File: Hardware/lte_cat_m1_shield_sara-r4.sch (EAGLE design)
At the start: 77 parts, among them J8 NANO_SIM, J9 U.FL, Q1 2.5A/30V/105mΩ, Q2 600mA/40V, U1 TXB0104, U2 3.3V, U3 MCP73831, U4 AP7361C-33FGE, U5 SARA-R4

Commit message: Minor revisions post-review
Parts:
- JP2: device SparkFun-Jumpers:JUMPER-SMT_3_NO_NO-SILK -> SparkFun-Jumpers:JUMPER-SMT_3_NO_SILK
- JP3, JP4, JP5, JP6: value JUMPER-SMT_2_NC_TRACE_NO-SILK -> JUMPER-SMT_2_NC_TRACE_SILK; device SparkFun-Jumpers:JUMPER-SMT_2_NC_TRACE_NO-SILK -> SparkFun-Jumpers:JUMPER-SMT_2_NC_TRACE_SILK
- JP7: device SparkFun-Jumpers:JUMPER-SMT_2_NO_NO-SILK -> SparkFun-Jumpers:JUMPER-SMT_2_NO_SILK
- U5: value SARA-R4 -> SARA-R410M-2B
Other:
- note added: "Hardware Serial Port (D0 = RX, D1 = TX)"
- note added: "If the Arduino does not supply IOREF, Use JP2 to set it to either 5V or 3.3V."
- note added: "Software serial port (D8 = RX, D9 = TX)"
- note removed: "If the Arduino does not supply IOREF, Use JP??? to set it to either 5V or 3.3V."
- moved on the sheet: C7, D3, R6, S1

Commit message: hardware revisions post u-blox review - x02 production hardware
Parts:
- R1: value 10k -> 47k; device SparkFun-Resistors:10KOHM-0603-1/10W-1% -> SparkFun-Resistors:47KOHM-0603-1/10W-1%
- U2: value 3.3V -> AP2112K-3.3
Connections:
- net D_N renamed D+
- net D_P renamed D-
- net GND: now also U5.RSVD@33
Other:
- note added: "Molex 146208 chip antenna peak gain: 698~960MHz: 0.2 dBi 1.7~2.7GHz: 3.8 dBi"
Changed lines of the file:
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@@
 <part name="GND41" library="SparkFun-PowerSymbols" deviceset="GND" device=""/>
 <part name="B1" library="SparkFun-Boards" deviceset="ARDUINO_UNO_R3_SHIELD" device="NOLABELS"/>
-<part name="U2" library="SparkFun-IC-Power" deviceset="V_REG_AP2112" device="K-3.3V" value="3.3V"/>
+<part name="U2" library="SparkFun-IC-Power" deviceset="V_REG_AP2112" device="K-3.3V" value="AP2112K-3.3"/>
 <part name="C2" library="SparkFun-Capacitors" deviceset="1.0UF" device="-0603-16V-10%" value="1.0uF"/>
 <part name="C4" library="SparkFun-Capacitors" deviceset="1.0UF" device="-0603-16V-10%" value="1.0uF"/>
 <part name="GND2" library="SparkFun-PowerSymbols" deviceset="GND" device=""/>
 <part name="GND9" library="SparkFun-PowerSymbols" deviceset="GND" device=""/>
-<part name="R1" library="SparkFun-Resistors" deviceset="10KOHM" device="-0603-1/10W-1%" value="10k"/>
+<part name="R1" library="SparkFun-Resistors" deviceset="47KOHM" device="-0603-1/10W-1%" value="47k"/>
 <part name="GND5" library="SparkFun-PowerSymbols" deviceset="GND" device=""/>
 <part name="GND6" library="SparkFun-PowerSymbols" deviceset="GND" device=""/>
@@
 </segment>
 </net>
-<net name="D_N" class="1">
+<net name="D+" class="1">
 <segment>
 <pinref part="D5" gate="G$1" pin="6"/>
@@
 </segment>
 </net>
-<net name="D_P" class="1">
+<net name="D-" class="1">
 <segment>
 <pinref part="D5" gate="G$1" pin="4"/>
@@
 SARA module are w/ respect
 to DTE (Arduino).</text>
+<text x="149.86" y="167.64" size="1.778" layer="97">Molex 146208 chip antenna peak gain:
+698~960MHz: 0.2 dBi
+1.7~2.7GHz: 3.8 dBi</text>
 </plain>
 <instances>
@@
 <instance part="S4" gate="G$1" x="33.02" y="121.92" rot="R90"/>
 <instance part="SUPPLY15" gate="G$1" x="63.5" y="22.86"/>
-<instance part="GND27" gate="1" x="63.5" y="68.58"/>
+<instance part="GND27" gate="1" x="63.5" y="58.42"/>
 <instance part="SUPPLY14" gate="G$1" x="60.96" y="142.24"/>
 <instance part="J8" gate="G$1" x="241.3" y="81.28"/>
@@
 <pinref part="U5" gate="G$1" pin="GND"/>
 <pinref part="GND27" gate="1" pin="GND"/>
-<wire x1="66.04" y1="73.66" x2="63.5" y2="73.66" width="0.1524" layer="91"/>
-<wire x1="63.5" y1="73.66" x2="63.5" y2="71.12" width="0.1524" layer="91"/>
+<wire x1="66.04" y1="63.5" x2="63.5" y2="63.5" width="0.1524" layer="91"/>
+<wire x1="63.5" y1="63.5" x2="63.5" y2="60.96" width="0.1524" layer="91"/>
+<pinref part="U5" gate="G$1" pin="RSVD@33"/>
+<wire x1="66.04" y1="68.58" x2="63.5" y2="68.58" width="0.1524" layer="91"/>
+<wire x1="63.5" y1="68.58" x2="63.5" y2="63.5" width="0.1524" layer="91"/>
+<junction x="63.5" y="63.5"/>
 </segment>
 <segment>
@@
 </segment>
 </net>
-<net name="D_N" class="1">
+<net name="D+" class="1">
 <segment>
 <pinref part="U5" gate="G$1" pin="USB_D-"/>
@@
 </segment>
 </net>
-<net name="D_P" class="1">
+<net name="D-" class="1">
 <segment>
 <pinref part="U5" gate="G$1" pin="USB_D+"/>

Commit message: v10 of the LTE Shield hardware.
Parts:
- removed U1: TXB0104, SparkFun-IC-Comms:TXB0104PWRSOIC14
- added U6: TCA9406DCU, ublox:TCA9406DCU
- added U8: TXB0104, SparkFun-IC-Comms:TXB0104PWR
- LOGO1: value SPARKX-LOGO4 -> SFE_LOGO_NAME.2_INCH; device SparkX:SPARKX-LOGO4 -> SparkFun-Aesthetics:SFE_LOGO_NAME.2_INCH
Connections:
- removed net GPIO3: J4.1, U5.GPIO3
- new net GPIO3-CELL: U5.GPIO3, U8.A1
- new net GPIO3-QWIIC: J4.1, U8.B1
- net 1.8V: now also U6.OE, U6.VCCA, U8.OE, U8.VCCA; no longer U1.OE, U1.VCCA
- net D+: now also D5.4, U5.USB_D+; no longer D5.6, U5.USB_D-
- net D-: now also D5.6, U5.USB_D-; no longer D5.4, U5.USB_D+
- net GND: now also U6.GND, U8.GND; no longer U1.GND
- net IOREF: now also U6.VCCB, U8.VCCB; no longer U1.VCCB
- net RX-ARDUINO: now also U8.B2; no longer U1.B3
- net RX-CELL: now also U8.A3; no longer U1.A4
- net SCL-CELL: now also U6.SCL_A; no longer U1.A1
- net SCL-QWIIC: now also U6.SCL_B; no longer U1.B1
- net SDA-CELL: now also U6.SDA_A; no longer U1.A2
- net SDA-QWIIC: now also U6.SDA_B; no longer U1.B2
- net TX-ARDUINO: now also U8.B3; no longer U1.B4
- net TX-CELL: now also U8.A2; no longer U1.A3
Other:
- note added: "GPIO3 is an optional interrupt output from the GPS module to the SARA module."
- note added: "v10"
- note removed: "GPIO3 is an (optional?) interrupt output from the GPS module to the SARA module."
- note removed: "x01"
- moved on the sheet: B1, C1, C3, J5, JP2, JP3, JP4, S1

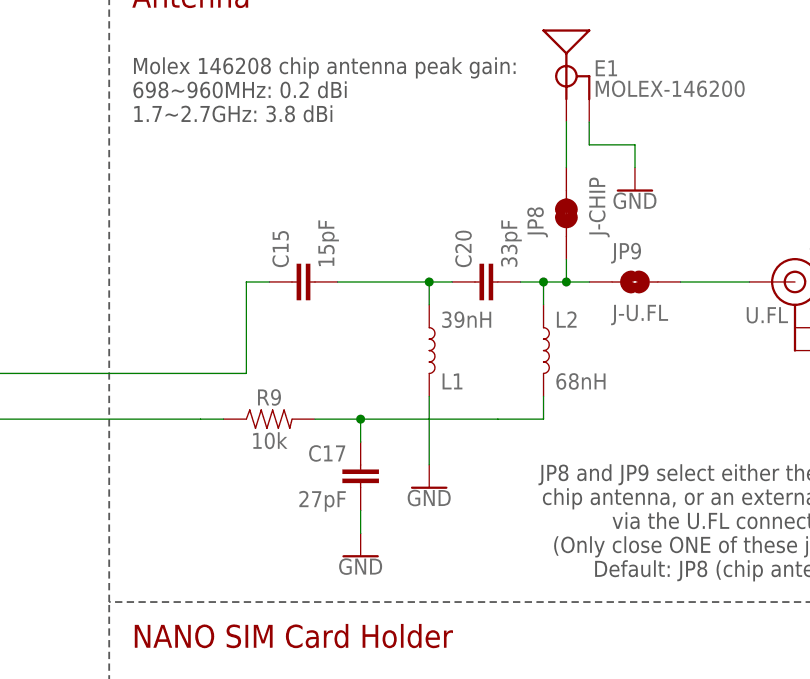
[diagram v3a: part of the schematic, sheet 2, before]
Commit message: DNP'ing the antenna-detect circuit.
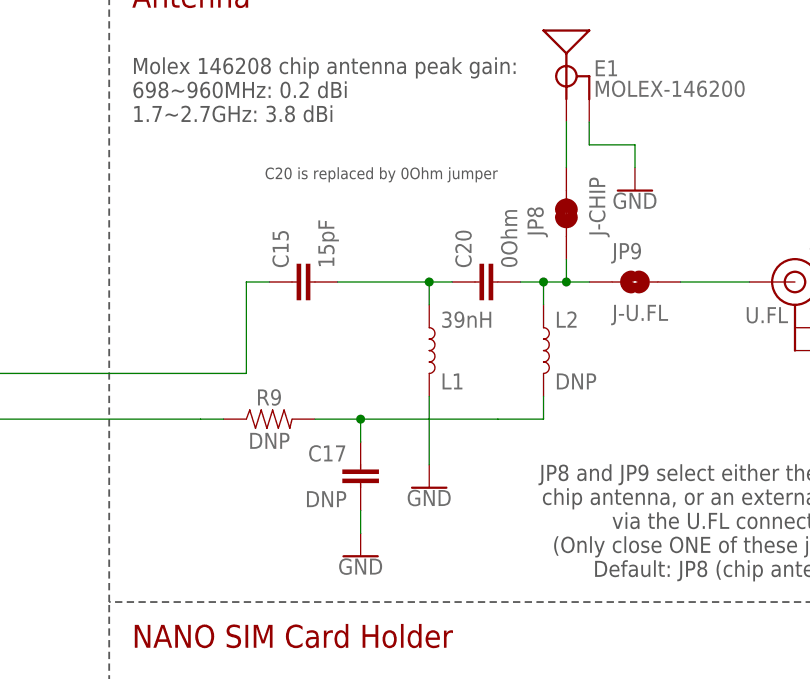
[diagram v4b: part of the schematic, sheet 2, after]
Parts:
- C17: value 27pF -> DNP
- C20: value 33pF -> 0Ohm
- L2: value 68nH -> DNP
- R9: value 10k -> DNP
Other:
- note added: "C20 is replaced by 0Ohm jumper"
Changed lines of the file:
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@@
 <grid distance="0.1" unitdist="inch" unit="inch" style="lines" multiple="1" display="no" altdistance="0.01" altunitdist="inch" altunit="inch"/>
 <layers>
-<layer number="1" name="Top" color="4" fill="1" visible="yes" active="no"/>
-<layer number="2" name="Route2" color="1" fill="3" visible="yes" active="no"/>
-<layer number="15" name="Route15" color="4" fill="6" visible="yes" active="no"/>
-<layer number="16" name="Bottom" color="1" fill="1" visible="yes" active="no"/>
-<layer number="17" name="Pads" color="2" fill="1" visible="yes" active="no"/>
-<layer number="18" name="Vias" color="2" fill="1" visible="yes" active="no"/>
-<layer number="19" name="Unrouted" color="6" fill="1" visible="yes" active="no"/>
-<layer number="20" name="Dimension" color="15" fill="1" visible="yes" active="no"/>
-<layer number="21" name="tPlace" color="16" fill="1" visible="yes" active="no"/>
-<layer number="22" name="bPlace" color="14" fill="1" visible="yes" active="no"/>
-<layer number="23" name="tOrigins" color="15" fill="1" visible="yes" active="no"/>
-<layer number="24" name="bOrigins" color="15" fill="1" visible="yes" active="no"/>
-<layer number="25" name="tNames" color="7" fill="1" visible="yes" active="no"/>
-<layer number="26" name="bNames" color="7" fill="1" visible="yes" active="no"/>
-<layer number="27" name="tValues" color="7" fill="1" visible="yes" active="no"/>
-<layer number="28" name="bValues" color="7" fill="1" visible="yes" active="no"/>
+<layer number="1" name="Top" color="4" fill="1" visible="no" active="no"/>
+<layer number="2" name="Route2" color="1" fill="3" visible="no" active="no"/>
+<layer number="15" name="Route15" color="4" fill="6" visible="no" active="no"/>
+<layer number="16" name="Bottom" color="1" fill="1" visible="no" active="no"/>
+<layer number="17" name="Pads" color="2" fill="1" visible="no" active="no"/>
+<layer number="18" name="Vias" color="2" fill="1" visible="no" active="no"/>
+<layer number="19" name="Unrouted" color="6" fill="1" visible="no" active="no"/>
+<layer number="20" name="Dimension" color="15" fill="1" visible="no" active="no"/>
+<layer number="21" name="tPlace" color="16" fill="1" visible="no" active="no"/>
+<layer number="22" name="bPlace" color="14" fill="1" visible="no" active="no"/>
+<layer number="23" name="tOrigins" color="15" fill="1" visible="no" active="no"/>
+<layer number="24" name="bOrigins" color="15" fill="1" visible="no" active="no"/>
+<layer number="25" name="tNames" color="7" fill="1" visible="no" active="no"/>
+<layer number="26" name="bNames" color="7" fill="1" visible="no" active="no"/>
+<layer number="27" name="tValues" color="7" fill="1" visible="no" active="no"/>
+<layer number="28" name="bValues" color="7" fill="1" visible="no" active="no"/>
 <layer number="29" name="tStop" color="7" fill="3" visible="no" active="no"/>
 <layer number="30" name="bStop" color="7" fill="6" visible="no" active="no"/>
@@
 <layer number="35" name="tGlue" color="7" fill="4" visible="no" active="no"/>
 <layer number="36" name="bGlue" color="7" fill="5" visible="no" active="no"/>
-<layer number="37" name="tTest" color="7" fill="1" visible="yes" active="no"/>
-<layer number="38" name="bTest" color="7" fill="1" visible="yes" active="no"/>
+<layer number="37" name="tTest" color="7" fill="1" visible="no" active="no"/>
+<layer number="38" name="bTest" color="7" fill="1" visible="no" active="no"/>
 <layer number="39" name="tKeepout" color="4" fill="11" visible="no" active="no"/>
 <layer number="40" name="bKeepout" color="1" fill="11" visible="no" active="no"/>
@@
 <layer number="44" name="Drills" color="7" fill="1" visible="no" active="no"/>
 <layer number="45" name="Holes" color="7" fill="1" visible="no" active="no"/>
-<layer number="46" name="Milling" color="3" fill="1" visible="yes" active="no"/>
-<layer number="47" name="Measures" color="7" fill="1" visible="yes" active="no"/>
-<layer number="48" name="Document" color="7" fill="1" visible="yes" active="no"/>
-<layer number="49" name="Reference" color="7" fill="1" visible="yes" active="no"/>
-<layer number="50" name="dxf" color="7" fill="1" visible="yes" active="no"/>
-<layer number="51" name="tDocu" color="6" fill="1" visible="yes" active="no"/>
-<layer number="52" name="bDocu" color="7" fill="1" visible="yes" active="no"/>
-<layer number="53" name="tGND_GNDA" color="7" fill="9" visible="yes" active="no"/>
-<layer number="54" name="bGND_GNDA" color="1" fill="9" visible="yes" active="no"/>
-<layer number="56" name="wert" color="7" fill="1" visible="yes" active="no"/>
-<layer number="57" name="tCAD" color="7" fill="1" visible="yes" active="no"/>
-<layer number="59" name="tCarbon" color="7" fill="1" visible="yes" active="no"/>
-<layer number="60" name="bCarbon" color="7" fill="1" visible="yes" active="no"/>
+<layer number="46" name="Milling" color="3" fill="1" visible="no" active="no"/>
+<layer number="47" name="Measures" color="7" fill="1" visible="no" active="no"/>
+<layer number="48" name="Document" color="7" fill="1" visible="no" active="no"/>
+<layer number="49" name="Reference" color="7" fill="1" visible="no" active="no"/>
+<layer number="50" name="dxf" color="7" fill="1" visible="no" active="no"/>
+<layer number="51" name="tDocu" color="6" fill="1" visible="no" active="no"/>
+<layer number="52" name="bDocu" color="7" fill="1" visible="no" active="no"/>
+<layer number="53" name="tGND_GNDA" color="7" fill="9" visible="no" active="no"/>
+<layer number="54" name="bGND_GNDA" color="1" fill="9" visible="no" active="no"/>
+<layer number="56" name="wert" color="7" fill="1" visible="no" active="no"/>
+<layer number="57" name="tCAD" color="7" fill="1" visible="no" active="no"/>
+<layer number="59" name="tCarbon" color="7" fill="1" visible="no" active="no"/>
+<layer number="60" name="bCarbon" color="7" fill="1" visible="no" active="no"/>
 <layer number="88" name="SimResults" color="9" fill="1" visible="yes" active="yes"/>
 <layer number="89" name="SimProbes" color="9" fill="1" visible="yes" active="yes"/>
@@
 <part name="GND34" library="SparkFun-PowerSymbols" deviceset="GND" device=""/>
 <part name="GND33" library="SparkFun-PowerSymbols" deviceset="GND" device=""/>
-<part name="C17" library="SparkFun-Capacitors" deviceset="27PF" device="-0603-50V-5%" value="27pF"/>
-<part name="R9" library="SparkFun-Resistors" deviceset="10KOHM" device="-0603-1/10W-1%" value="10k"/>
+<part name="C17" library="SparkFun-Capacitors" deviceset="27PF" device="-0603-50V-5%" value="DNP"/>
+<part name="R9" library="SparkFun-Resistors" deviceset="10KOHM" device="-0603-1/10W-1%" value="DNP"/>
 <part name="GND36" library="SparkFun-PowerSymbols" deviceset="GND" device=""/>
 <part name="C15" library="SparkFun-Capacitors" deviceset="15PF" device="-0603-50V-5%" value="15pF"/>
-<part name="C20" library="SparkFun-Capacitors" deviceset="33PF" device="-0603-50V-5%" value="33pF"/>
+<part name="C20" library="SparkFun-Capacitors" deviceset="33PF" device="-0603-50V-5%" value="0Ohm"/>
 <part name="GND42" library="SparkFun-PowerSymbols" deviceset="GND" device=""/>
 <part name="L1" library="ublox" deviceset="INDUCTOR" device="-0603-39NH" value="39nH"/>
 <part name="GND38" library="SparkFun-PowerSymbols" deviceset="GND" device=""/>
-<part name="L2" library="ublox" deviceset="INDUCTOR" device="-0603-68NH" value="68nH"/>
+<part name="L2" library="ublox" deviceset="INDUCTOR" device="-0603-68NH" value="DNP"/>
 <part name="Q2" library="SparkFun-DiscreteSemi" deviceset="TRANS_NPN" device="-MMBT2222AL" value="600mA/40V"/>
 <part name="SUPPLY21" library="SparkFun-PowerSymbols" deviceset="3.3V" device=""/>
@@
 698~960MHz: 0.2 dBi
 1.7~2.7GHz: 3.8 dBi</text>
+<text x="190.5" y="162.56" size="1.27" layer="97" rot="R180">C20 is replaced by 0Ohm jumper</text>
 </plain>
 <instances>

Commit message: Revisions post-checklist.
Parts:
- removed JP9: J-U.FL, SparkFun-Jumpers:JUMPER-SMT_2_NO_NO-SILK
- removed R9: DNP, SparkFun-Resistors:10KOHM-0603-1/10W-1%
- added JP1: IOREF-SEL, SparkFun-Jumpers:JUMPER-SMT_3_NO_SILK
- added LOGO3: SFE_LOGO_NAME.2_INCH, SparkFun-Aesthetics:SFE_LOGO_NAME.2_INCH
- added R4: 10k, SparkFun-Resistors:10KOHM-0603-1/10W-1%
- C1, C3: value 0.1uF -> 1.0uF; device SparkFun-Capacitors:0.1UF-0603-25V-(+80/-20%) -> SparkFun-Capacitors:1.0UF-0603-16V-10%
- C16: value 47pF -> DNP; device SparkFun-Capacitors:47PF-0603-50V-5% -> SparkFun-Capacitors:27PF-0603-50V-5%
- C17: value DNP -> 47pF; device SparkFun-Capacitors:27PF-0603-50V-5% -> SparkFun-Capacitors:47PF-0603-50V-5%
- C19: value 47pF -> 0Ohm; device SparkFun-Capacitors:47PF-0603-50V-5% -> SparkFun-Capacitors:33PF-0603-50V-5%
- C2, C4: value 1.0uF -> 0.1uF; device SparkFun-Capacitors:1.0UF-0603-16V-10% -> SparkFun-Capacitors:0.1UF-0603-25V-(+80/-20%)
- C20: value 0Ohm -> 47pF; device SparkFun-Capacitors:33PF-0603-50V-5% -> SparkFun-Capacitors:47PF-0603-50V-5%
- D1: value Yellow -> PRTR5V0U2F; device SparkFun-LED:LED-YELLOW0603 -> ublox:PRTR5V0U2F
- D2: value 1A/23V/620mV -> Yellow; device SparkFun-DiscreteSemi:DIODE-SCHOTTKY-BAT20J -> SparkFun-LED:LED-YELLOW0603
- D3: value RED -> 1A/23V/620mV; device SparkFun-LED:LED-RED0603 -> SparkFun-DiscreteSemi:DIODE-SCHOTTKY-BAT20J
- D4: value BLUE -> RED; device SparkFun-LED:LED-BLUE0603 -> SparkFun-LED:LED-RED0603
- D5: value PRTR5V0U2F -> BLUE; device ublox:PRTR5V0U2F -> SparkFun-LED:LED-BLUE0603
- J8: value NANO_SIM -> U.FL; device ublox:NANO_SIMWURTH -> SparkFun-Connectors:U.FL
- J9: value U.FL -> NANO_SIM; device SparkFun-Connectors:U.FL -> ublox:NANO_SIMWURTH
- JP2: value IOREF-SEL -> JUMPER-SMT_2_NC_TRACE_SILK; device SparkFun-Jumpers:JUMPER-SMT_3_NO_SILK -> SparkFun-Jumpers:JUMPER-SMT_2_NC_TRACE_SILK
- JP6: value JUMPER-SMT_2_NC_TRACE_SILK -> VUSB_DET; device SparkFun-Jumpers:JUMPER-SMT_2_NC_TRACE_SILK -> SparkFun-Jumpers:JUMPER-SMT_2_NO_SILK
- JP7: value VUSB_DET -> J-CHIP; device SparkFun-Jumpers:JUMPER-SMT_2_NO_SILK -> SparkFun-Jumpers:JUMPER-SMT_2_NC_TRACE_NO-SILK
- JP8: value J-CHIP -> J-U.FL; device SparkFun-Jumpers:JUMPER-SMT_2_NC_TRACE_NO-SILK -> SparkFun-Jumpers:JUMPER-SMT_2_NO_NO-SILK
- R5, R7: value 10k -> 1k; device SparkFun-Resistors:10KOHM-0603-1/10W-1% -> SparkFun-Resistors:1KOHM-0603-1/10W-1%
- R6: value 1k -> 10k; device SparkFun-Resistors:1KOHM-0603-1/10W-1% -> SparkFun-Resistors:10KOHM-0603-1/10W-1%
- R8: value 1k -> DNP; device SparkFun-Resistors:1KOHM-0603-1/10W-1% -> SparkFun-Resistors:10KOHM-0603-1/10W-1%
- U4: value AP7361C-33FGE -> TCA9406DCU; device ublox:AP7361C-33FGE -> ublox:TCA9406DCU
- U5: value SARA-R410M-2B -> AP7361C-33FGE; device ublox:SARA-R4 -> ublox:AP7361C-33FGE
- U6: value TCA9406DCU -> SARA-R410M-2B; device ublox:TCA9406DCU -> ublox:SARA-R4
- renumbered D7 to D6, U8 to U1
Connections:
- net 1.8V: now also C4.1, U4.OE, U4.VCCA, U6.V_INT; no longer C1.1, U5.V_INT, U6.OE, U6.VCCA
- net 3.3V: now also C1.1, D5.A, R5.2, U5.OUT, U6.VCC; no longer C2.1, D4.A, R6.2, U4.OUT, U5.VCC
- net ANT: now also U6.ANT; no longer U5.ANT
- net ANT_DET: now also R8.1, U6.ANT_DET; no longer R9.1, U5.ANT_DET
- net ARDUINO-3.3V: now also JP1.3; no longer JP2.3
- net ARDUINO-5V: now also JP1.1; no longer JP2.1
- net CTS: now also U6.CTS; no longer U5.CTS
- net D+: now also D1.4, U6.USB_D+; no longer D5.4, U5.USB_D+
- net D-: now also D1.6, U6.USB_D-; no longer D5.6, U5.USB_D-
- net DCD: now also U6.DCD; no longer U5.DCD
- net DSR: now also U6.DSR; no longer U5.DSR
- net DTR: now also JP5.2, U6.DTR; no longer JP6.2, U5.DTR
- net GND: now also C20.2, D1.2, D4.C, J8.GND@0, J8.GND@1, J9.GND, JP4.1, R4.1, U6.RSVD@33; no longer C19.2, D3.C, D5.2, J8.GND, J9.GND@0, J9.GND@1, JP6.1, R5.1, U5.RSVD@33
- net GPIO1: now also R6.2, U6.GPIO1; no longer R7.2, U5.GPIO1
- net GPIO2: now also U6.GPIO2; no longer U5.GPIO2
- net GPIO3-CELL: now also U6.GPIO3; no longer U5.GPIO3
- net GPS-3.3V: now also C3.1; no longer C4.1
- net IOREF: now also C2.1, JP1.2, U4.VCCB; no longer C3.1, JP2.2, U6.VCCB
- net N$10: now also R6.1; no longer R7.1
- net N$12: now also D1.1; no longer D5.1
- net N$13: now also D5.C, R7.2; no longer D4.C, R8.2
- net N$14: now also D1.3; no longer D5.3
- net N$15: now also R7.1; no longer R8.1
- net N$16: now also D4.A, R5.1; no longer D3.A, R6.1
- net N$17: now also D2.C; no longer D1.C
- net N$19: now also JP2.1; no longer JP3.1
- net N$20: now also JP3.1; no longer JP4.1
- net N$21: now also C19.2, JP7.1; no longer C20.2, JP9.1
- net N$22: now also JP7.2; no longer JP8.2
- net N$7: now also C16.1, R8.2; no longer C17.1, R9.2
- net N$8: now also C19.1; no longer C20.1
- net N$9: now also J8.SIGNAL, JP8.2; no longer J9.SIGNAL, JP9.2
- net PWR_ON: now also JP2.2, U6.PWR_ON; no longer JP3.2, U5.PWR_ON
- net RESET_N: now also JP3.2, U6.RESET_N; no longer JP4.2, U5.RESET_N
- net RI: now also U6.RI; no longer U5.RI
- net RTS: now also JP4.2, U6.RTS; no longer JP5.2, U5.RTS
- net RX-CELL: now also U6.TXD; no longer U5.TXD
- net SCL-CELL: now also U4.SCL_A, U6.SCL; no longer U5.SCL, U6.SCL_A
- net SCL-QWIIC: now also U4.SCL_B; no longer U6.SCL_B
- net SDA-CELL: now also U4.SDA_A, U6.SDA; no longer U5.SDA, U6.SDA_A
- net SDA-QWIIC: now also U4.SDA_B; no longer U6.SDA_B
- net SIM_CLK: now also J9.CLK, U6.SIM_CLK; no longer J8.CLK, U5.SIM_CLK
- net SIM_IO: now also C17.1, J9.IO, U6.SIM_IO; no longer C16.1, J8.IO, U5.SIM_IO
- net SIM_RST: now also C20.1, J9.RST, U6.SIM_RST; no longer C19.1, J8.RST, U5.SIM_RST
- net TX-CELL: now also U6.RXD; no longer U5.RXD
- net VIN: now also D3.C, U5.EN, U5.IN; no longer D2.C, U4.EN, U4.IN
- net VSIM: now also J9.VCC, U6.VSIM; no longer J8.VCC, U5.VSIM
- net VUSB_DET: now also JP6.2, U6.VUSB_DET; no longer JP7.2, U5.VUSB_DET
- net V_USB: now also D1.5, D3.A, JP6.1, R4.2; no longer D1.A, D5.5, JP7.1, R5.2
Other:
- note added: "If the Arduino does not supply IOREF, Use JP1 to set it to either 5V or 3.3V."
- note added: "JP2 and JP3 can disconnect control lines from Arduino."
- note added: "JP4 and JP5 short RTS and DTR to GND. This is the recommended configuration for a UART with NO FLOW CONTROL."
- note added: "JP7 and JP8 select either the on-board chip antenna, or an external antenna via the U.FL connector. (Only close ONE of these jumpers!) Default: JP8 (chip antenna)"
- note added: "Must be enabled with: AT+UGPIOC=16,2"
- note added: "Note: UART RX/TX pin names on SARA module are w/ respect to DTE (Arduino)."
- note added: "SARA-R410M-02B ============== VCC Range: 3.2-4.2V Max current: 490mA (Peak Cat M1 Tx) Avg. current: 190mA (Cat M1 Tx/Rx)"
- note added: "To enable the SARA module's USB interface, close JP6. (UART cannot be used while USB is connected!)"
- note removed: "If the Arduino does not supply IOREF, Use JP2 to set it to either 5V or 3.3V."
- note removed: "JP5 and JP6 short RTS and DTR to GND. This is the recommended configuration for a UART with NO FLOW CONTROL."
- note removed: "JP8 and JP9 select either the on-board chip antenna, or an external antenna via the U.FL connector. (Only close ONE of these jumpers!) Default: JP8 (chip antenna)"
- note removed: "To enable the SARA module's USB interface, close JP7. (UART cannot be used while USB is connected!)"
- note removed: "UART RX/TX pin names on SARA module are w/ respect to DTE (Arduino)."
- note removed: "VCC range: 3.2-4.2V"
- moved on the sheet: C1, C16, C17, C19, C2, C20, C3, C4, C5, C6, C7, JP3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
